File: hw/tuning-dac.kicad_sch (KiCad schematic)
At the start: 16 parts

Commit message: Rx path is getting closer. Differential LO outputs from VFO. Clean up.
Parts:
- gave numbers to parts that had none: 10
- renumbered R2 to R702, R3 to R703, R4 to R704, R6 to R706, R7 to R707, R8 to R708
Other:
- note added: "Varactor tuning range is 30..435pF in 0..7V. Multiply DAC output by 3.5: x2 in DAC gain x1.75 in buffer amp."
- note removed: "Varactor tuning range is 30..435pF in 0..7V. Need to multiply DAC value by 3.5 (x2 in DAC gain and x1.75 in buffer amp)"

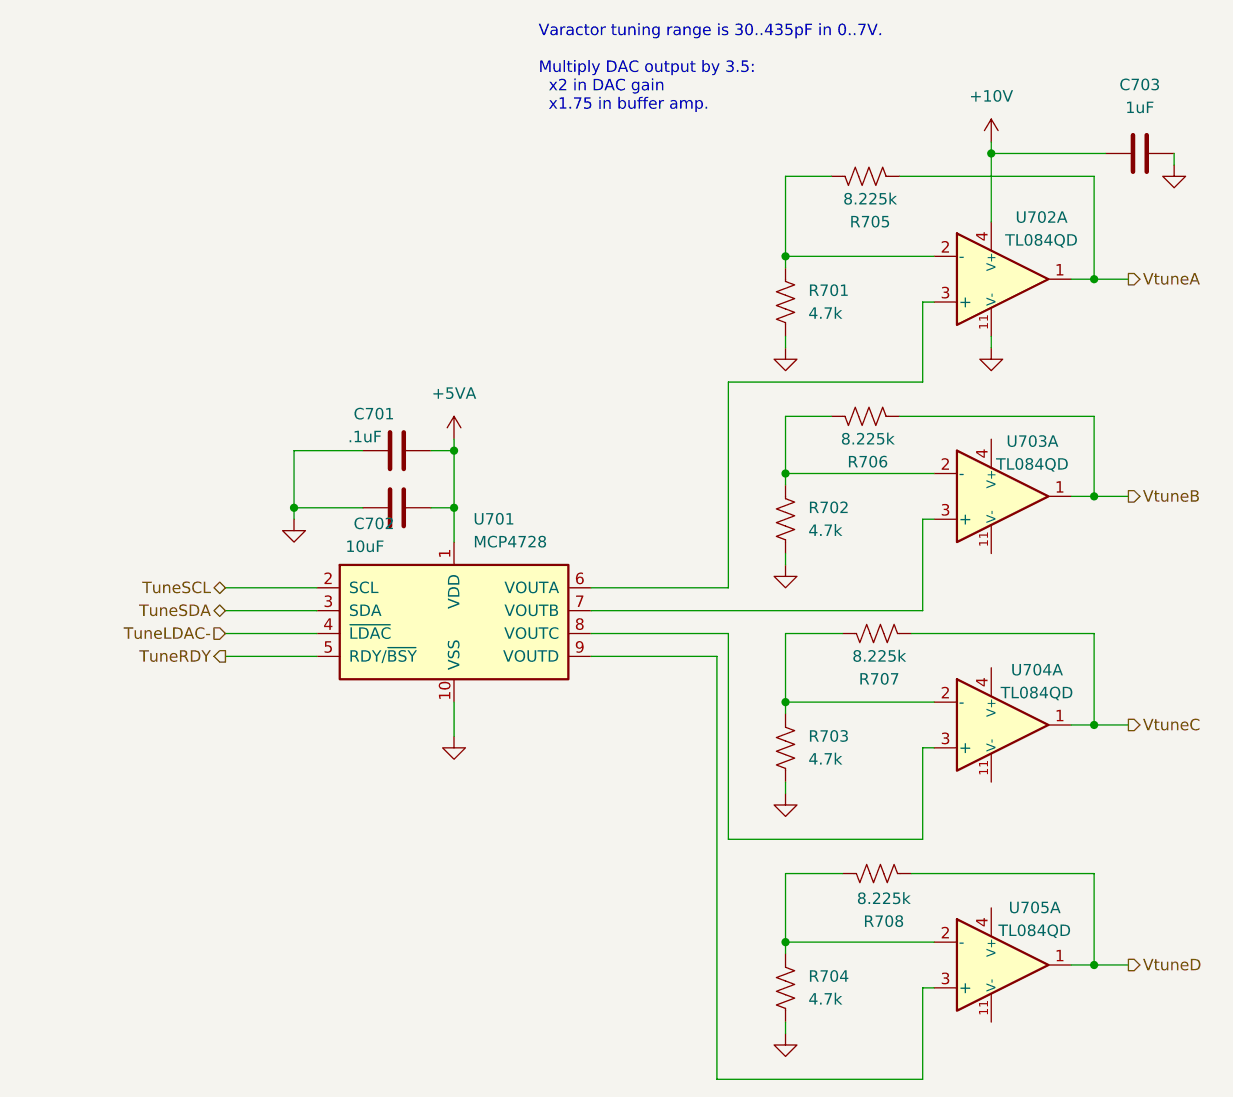
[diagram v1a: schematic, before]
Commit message: Checkpoint. More of rx path done. VFOs are now LVDS. Starting USB and power.
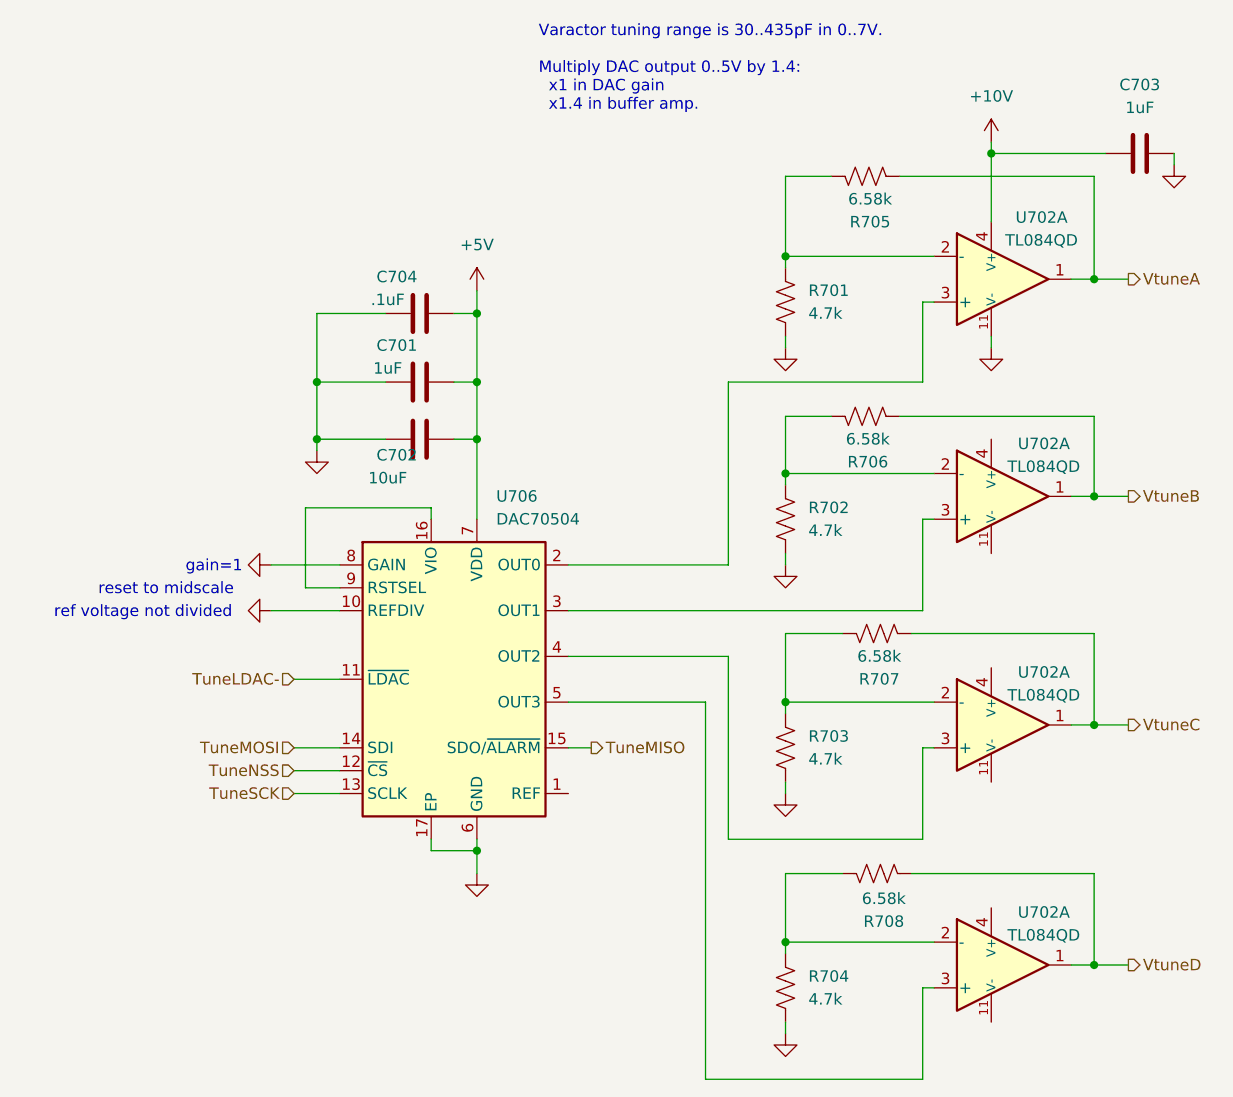
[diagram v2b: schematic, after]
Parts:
- removed U701: MCP4728, Package_SO:MSOP-10_3x3mm_P0.5mm, symbol Analog_DAC:MCP4728
- removed U703, U704, U705: TL084QD, PCM_Package_SO_AKL:SOIC-14_3.9x8.7mm_P1.27mm, symbol PCM_Amplifier_Operational_AKL:TL084QD
- added C704: .1uF, symbol Device:C
- added U706: DAC70504, Package_DFN_QFN:Texas_RTE0016D_WQFN-16-1EP_3x3mm_P0.5mm_EP0.8x0.8mm_ThermalVias, symbol Analog_DAC:DAC70504
- C701: value .1uF -> 1uF
- R705, R706, R707, R708: value 8.225k -> 6.58k
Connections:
- net GND: now also C704.1, U706.10 (REFDIV), U706.17 (EP), U706.6 (GND), U706.8 (GAIN)
- net TuneLDAC-: now also U706.11 (~{LDAC})
- net VtuneB: now also U702.1
- net VtuneC: now also U702.1
- net VtuneD: now also U702.1
- net at R702.1, R706.1: now also U702.2 (-)
- net at R703.1, R707.1: now also U702.2 (-)
- net at R704.1, R708.1: now also U702.2 (-)
- net at U702.3 (+): now also U706.5 (OUT3)
- net +5VA renamed +5V
- net +5V: now also C704.2, U706.7 (VDD)
- new net: U702.3 (+), U706.2 (OUT0)
- new net: U702.3 (+), U706.3 (OUT1)
- new net: U702.3 (+), U706.4 (OUT2)
- new net: U706.16 (VIO), U706.9 (RSTSEL)
- new net TuneMISO: U706.15 (SDO/~{ALARM})
- new net TuneMOSI: U706.14 (SDI)
- new net TuneNSS: U706.12 (~{CS})
- new net TuneSCK: U706.13 (SCLK)
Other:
- note added: "Varactor tuning range is 30..435pF in 0..7V. Multiply DAC output 0..5V by 1.4: x1 in DAC gain x1.4 in buffer amp."
- note added: "gain=1"
- note added: "ref voltage not divided"
- note added: "reset to midscale"
- note removed: "Varactor tuning range is 30..435pF in 0..7V. Multiply DAC output by 3.5: x2 in DAC gain x1.75 in buffer amp."
- moved on the sheet: C701, C702, U702A

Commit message: Restructure power and USB sheets a bit. Generate each power rail we need so far from USB VBUS, but still need to control VBUS input with TI USBPD chip. Set up USB2 data net class and power and GND netclasses.
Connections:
- no-connect marks 0 -> 1
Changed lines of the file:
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@@
 	(title_block
 		(title "Tuning DAC")
-		(date "2025-03-25")
+		(date "2025-03-26")
 		(company "SoftShack")
 		(comment 1 "Alan Mimms")
@@
 		(color 0 0 0 0)
 	)
+	(no_connect
+		(at 80.01 102.87)
+	)
 	(wire

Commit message: Checkpoint before resuming project
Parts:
- added U702, U703, U704: TL084QD, PCM_Package_SO_AKL:SOIC-14_3.9x8.7mm_P1.27mm, symbol PCM_Amplifier_Operational_AKL:TL084QD
- renumbered C704 to C701, C701 to C702, C702 to C703, C703 to C704, U706 to U701, U702 to U704
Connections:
- net +10V: now also U702.4 (V+); no longer U704.4 (V+)
- net GND: now also U702.11 (V-); no longer U704.11 (V-)
- net VtuneA: now also U702.1; no longer U704.1
- net VtuneB: now also U703.1; no longer U704.1
- net VtuneC: now also U704.1; no longer U704.1
- net at R702.1, R706.1: now also U703.2 (-); no longer U704.2 (-)
- net at R703.1, R707.1: now also U704.2 (-); no longer U704.2 (-)
- net at R701.1, R705.1: now also U702.2 (-); no longer U704.2 (-)
- net at U704.3 (+): now also U701.5 (OUT3); no longer U701.2 (OUT0)
- net at U701.3 (OUT1): now also U703.3 (+); no longer U704.3 (+)
- net at U701.4 (OUT2): now also U704.3 (+); no longer U704.3 (+)
- new net: U701.2 (OUT0), U702.3 (+)

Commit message: Working on multi-band BPF and switching
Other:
- company: SoftShack -> WB7NAB
- title: Tuning DAC -> ${title}
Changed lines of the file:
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@@
 	(generator "eeschema")
 	(generator_version "9.0")
-	(paper "A")
+	(paper "USLetter")
 	(title_block
-		(title "Tuning DAC")
-		(date "2025-03-26")
-		(company "SoftShack")
+		(title "${title}")
+		(date "2025-08-10")
+		(company "WB7NAB")
 		(comment 1 "Alan Mimms")
-		(comment 2 "WB7NAB")
 	)
 	(text "Varactor tuning range is 30..435pF in 0..7V.\n\nMultiply DAC output 0..5V by 1.4:\n  x1 in DAC gain\n  x1.4 in buffer amp."

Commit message: Starting to build BPFs for 7 bands
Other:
- title: ${title} -> Tuning DAC
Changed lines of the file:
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@@
 	(paper "USLetter")
 	(title_block
-		(title "${title}")
+		(title "Tuning DAC")
 		(date "2025-08-10")
 		(company "WB7NAB")
